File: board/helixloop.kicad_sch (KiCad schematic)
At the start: 17 parts, among them J1 Conn_01x04, J2 Conn_01x02

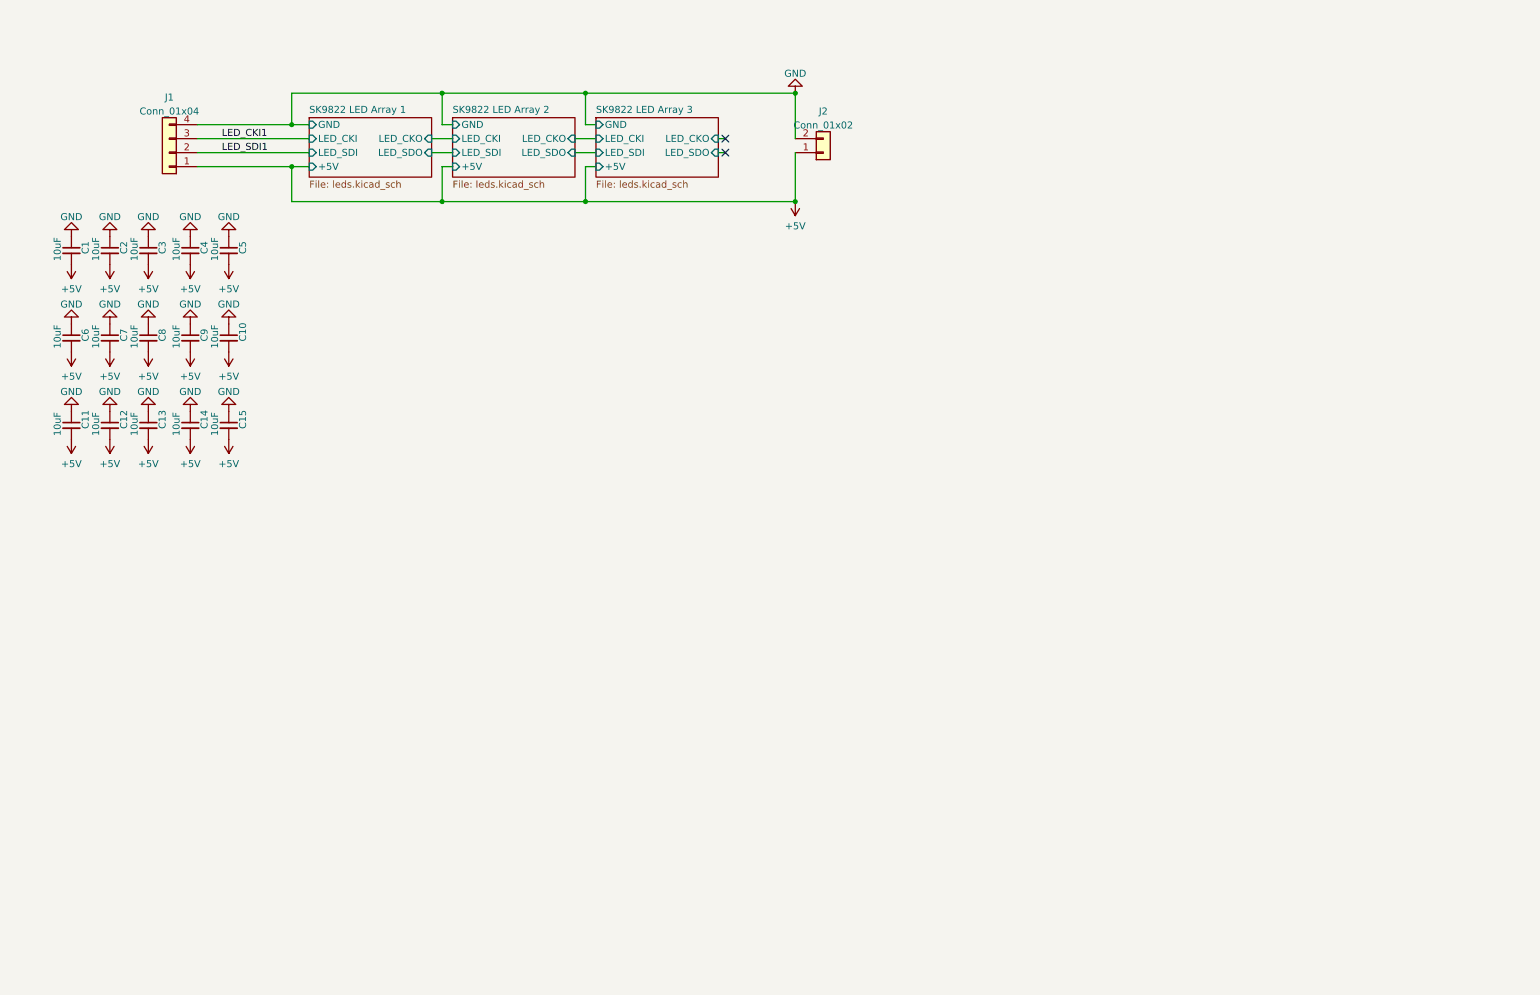
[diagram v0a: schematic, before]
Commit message: v2 concept: add an rp2040, microphone, usb port; rotate entire design 1/12 turn to help align usb port and led data in; rough layout
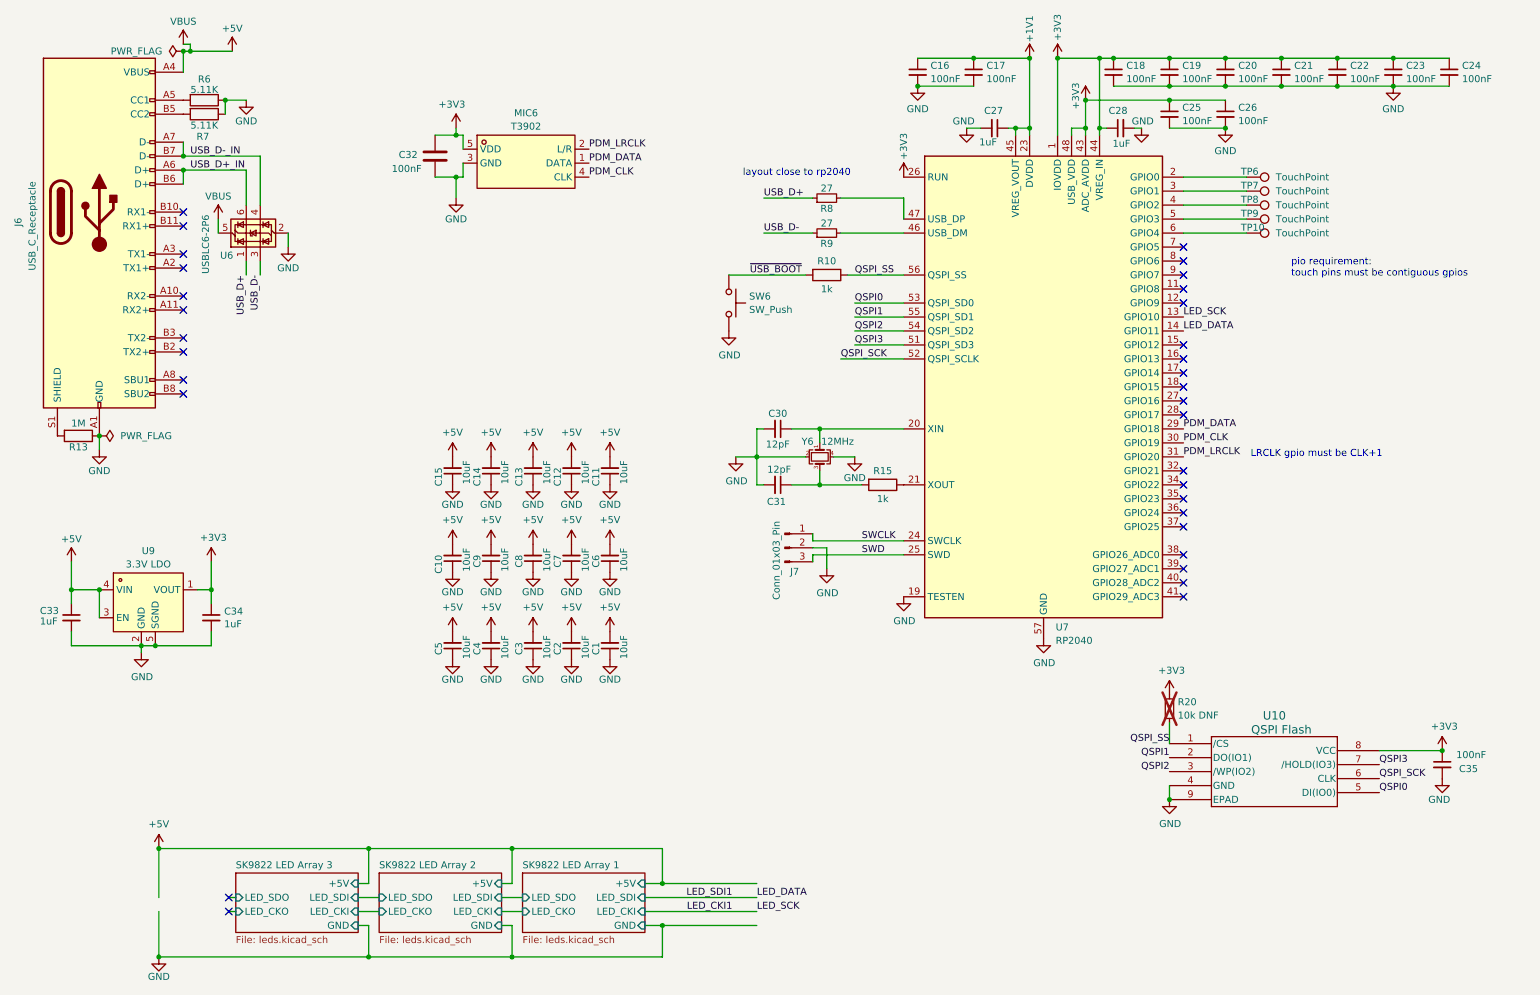
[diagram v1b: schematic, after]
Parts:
- removed J1: Conn_01x04, helixloop:SMD_Pad_01x04_2.54mm, symbol Connector_Generic:Conn_01x04
- removed J2: Conn_01x02, helixloop:SMD_Pad_01x02_2.54mm, symbol Connector_Generic:Conn_01x02
- added C16, C17, C18, C19, C20, C21, C22, C23, C24, C25, C26, C35: 100nF, Capacitor_SMD:C_0402_1005Metric, symbol Device:C_Small
- added C27, C28, C33, C34: 1uF, Capacitor_SMD:C_0402_1005Metric, symbol Device:C_Small
- added C30, C31: 12pF, Capacitor_SMD:C_0402_1005Metric, symbol Device:C_Small
- added C32: 100nF, Capacitor_SMD:C_0402_1005Metric, symbol Device:C
- added J6: USB_C_Receptacle, helixloop:USB-SMD_USB-TYPE-C-020, symbol Connector:USB_C_Receptacle
- added J7: Conn_01x03_Pin, penta:SMD_Pad_01x03_1.27mm, symbol Connector:Conn_01x03_Pin
- added MIC6: T3902, helixloop:MIC_T3902, symbol penta:MMICT390200012
- added R10, R15: 1k, Resistor_SMD:R_0402_1005Metric, symbol Device:R
- added R13: 1M, Resistor_SMD:R_0402_1005Metric, symbol Device:R
- added R20: 10k DNF, Resistor_SMD:R_0402_1005Metric, symbol Device:R_Small
- added R6, R7: 5.11K, Resistor_SMD:R_0402_1005Metric, symbol Device:R
- added R8, R9: 27, Resistor_SMD:R_0402_1005Metric, symbol Device:R_Small
- added SW6: SW_Push, helixloop:KEY-SMD_L3.0-W2.5-LS4.0, symbol Switch:SW_Push
- added TP10, TP6, TP7, TP8, TP9: TouchPoint, penta:ScrewTouchHole, symbol Connector:TestPoint
- added U10: QSPI Flash, helixloop:USON_3X2_WIN, symbol helixloop:QSPI Flash
- added U6: USBLC6-2P6, Package_TO_SOT_SMD:SOT-666, symbol Power_Protection:USBLC6-2P6
- added U7: RP2040, Package_DFN_QFN:QFN-56-1EP_7x7mm_P0.4mm_EP3.2x3.2mm, symbol MCU_RaspberryPi:RP2040
- added U9: 3.3V LDO, Package_DFN_QFN:OnSemi_XDFN4-1EP_1.0x1.0mm_EP0.52x0.52mm, symbol helixloop:RT9078-33GQZ
- added Y6: 12MHz, Crystal:Crystal_SMD_2520-4Pin_2.5x2.0mm, symbol Device:Crystal_GND24_Small
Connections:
- net +5V: now also C33.1, J6.A4 (VBUS), J6.A9 (VBUS), J6.B4 (VBUS), J6.B9 (VBUS), U6.5 (VBUS), U9.3 (EN), U9.4 (VIN)
- net GND: now also C16.2, C17.2, C18.2, C19.2, C20.2, C21.2, C22.2, C23.2, C24.2, C25.2, C26.2, C27.2, C28.2, C30.2, C31.2, C32.2, C33.2, C34.2, C35.2, J6.A1 (GND), J6.A12 (GND), J6.B1 (GND), J6.B12 (GND), J7.2 (Pin_2), MIC6.3 (GND), R13.1, R6.1, R7.1, SW6.2, U10.4 (GND), U10.9 (EPAD), U6.2 (GND), U7.19 (TESTEN), U7.57 (GND), U9.2 (GND), U9.5 (SGND), Y6.2, Y6.4
- net LED_CKI1: now also U7.13 (GPIO10)
- new net: TP7.1, U7.3 (GPIO1)
- new net: C31.1, R15.2, Y6.3
- new net: TP10.1, U7.6 (GPIO4)
- new net: TP6.1, U7.2 (GPIO0)
- new net: C30.1, U7.20 (XIN), Y6.1
- new net: R15.1, U7.21 (XOUT)
- new net: TP8.1, U7.4 (GPIO2)
- new net: R9.2, U7.46 (USB_DM)
- new net: R8.2, U7.47 (USB_DP)
- new net: TP9.1, U7.5 (GPIO3)
- new net: J6.B5 (CC2), R7.2
- new net: J6.S1 (SHIELD), R13.2
- new net: J6.A5 (CC1), R6.2
- new net +1V1: C16.1, C17.1, C27.1, U7.23 (DVDD), U7.45 (VREG_VOUT), U7.50 (DVDD)
- new net +3V3: C18.1, C19.1, C20.1, C21.1, C22.1, C23.1, C24.1, C25.1, C26.1, C28.1, C32.1, C34.1, C35.1, MIC6.5 (VDD), R20.1, U10.8 (VCC), U7.1 (IOVDD), U7.10 (IOVDD), U7.22 (IOVDD), U7.26 (RUN), U7.33 (IOVDD), U7.42 (IOVDD), U7.43 (ADC_AVDD), U7.44 (VREG_IN), U7.48 (USB_VDD), U7.49 (IOVDD), U9.1 (VOUT)
- new net LED_DATA: U7.14 (GPIO11)
- new net PDM_CLK: MIC6.4 (CLK), U7.30 (GPIO19)
- new net PDM_DATA: MIC6.1 (DATA), U7.29 (GPIO18)
- new net PDM_LRCLK: MIC6.2 (L/R), U7.31 (GPIO20)
- new net QSPI0: U10.5 (DI(IO0)), U7.53 (QSPI_SD0)
- new net QSPI1: U10.2 (DO(IO1)), U7.55 (QSPI_SD1)
- new net QSPI2: U10.3 (/WP(IO2)), U7.54 (QSPI_SD2)
- new net QSPI3: U10.7 (/HOLD(IO3)), U7.51 (QSPI_SD3)
- new net QSPI_SCK: U10.6 (CLK), U7.52 (QSPI_SCLK)
- new net QSPI_SS: R10.1, R20.2, U10.1 (/CS), U7.56 (QSPI_SS)
- new net SWCLK: J7.1 (Pin_1), U7.24 (SWCLK)
- new net SWD: J7.3 (Pin_3), U7.25 (SWD)
- new net USB_D+: R8.1, U6.1 (I/O1)
- new net USB_D+_IN: J6.A6 (D+), J6.B6 (D+), U6.6 (I/O1)
- new net USB_D-: R9.1, U6.3 (I/O2)
- new net USB_D-_IN: J6.A7 (D-), J6.B7 (D-), U6.4 (I/O2)
- new net ~{USB_BOOT}: R10.2, SW6.1
- no-connect marks 2 -> 32
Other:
- note added: "LRCLK gpio must be CLK+1"
- note added: "layout close to rp2040"
- note added: "pio requirement: touch pins must be contiguous gpios"
- moved on the sheet: C1, C10, C11, C12, C13, C14, C15, C2, C3, C4, C5, C6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

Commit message: add a 5v copper layer on top; add more 5v capacitance; layout improvements
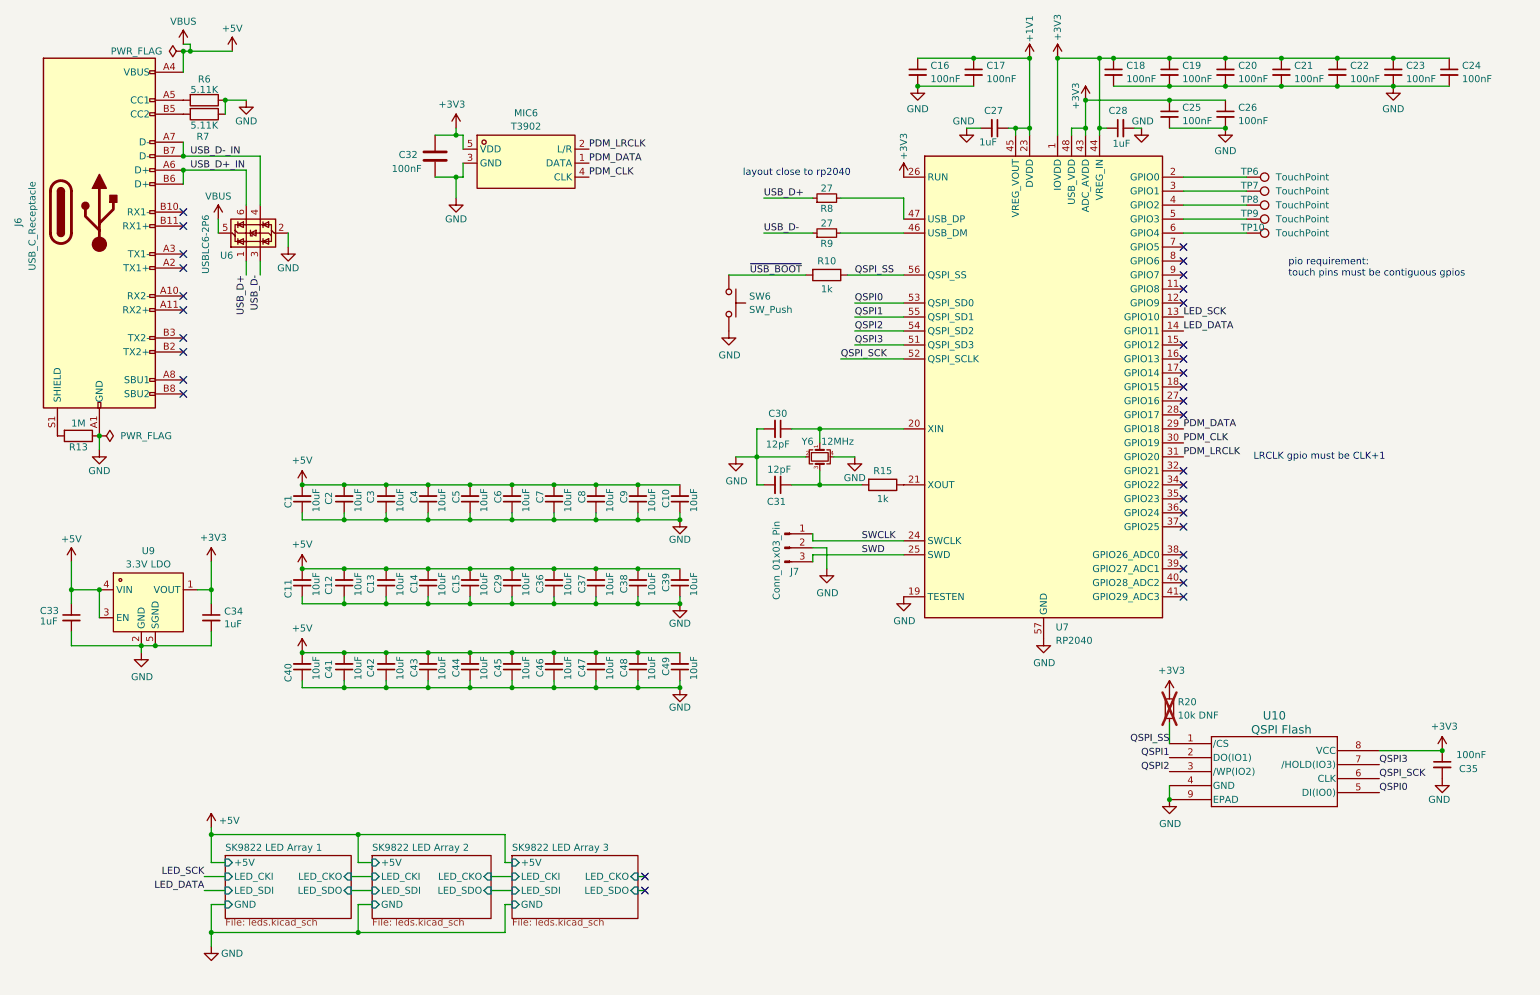
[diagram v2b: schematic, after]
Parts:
- removed C1, C2, C3, C4, C5: 10uF, Capacitor_SMD:C_0402_1005Metric, symbol Device:C_Small
- added C11, C12, C13, C14, C15, C29, C36, C37, C38, C39, C40, C41, C42, C43, C44, C45, C46, C47, C48, C49: 10uF, Capacitor_SMD:C_0402_1005Metric, symbol Device:C_Small
- renumbered C15 to C1, C14 to C2, C13 to C3, C12 to C4, C11 to C5
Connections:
- net +5V: now also C11.2, C12.2, C13.2, C14.2, C15.2, C29.2, C36.2, C37.2, C38.2, C39.2, C40.2, C41.2, C42.2, C43.2, C44.2, C45.2, C46.2, C47.2, C48.2, C49.2
- net GND: now also C11.1, C12.1, C13.1, C14.1, C15.1, C29.1, C36.1, C37.1, C38.1, C39.1, C40.1, C41.1, C42.1, C43.1, C44.1, C45.1, C46.1, C47.1, C48.1, C49.1
- net LED_CKI1 renamed LED_SCK
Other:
- moved on the sheet: C1, C2, C3, C4, C5

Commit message: mostly fix ERC
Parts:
- removed C32: 100nF, Capacitor_SMD:C_0402_1005Metric, symbol Device:C
- removed TP6, TP7: TouchPoint, penta:ScrewTouchHole, symbol Connector:TestPoint
- added C32: 100nF, Capacitor_SMD:C_0402_1005Metric, symbol Device:C_Small
- MIC6: footprint helixloop:MIC_T3902 -> easyeda2kicad:MIC-SMD_5P-L3.5-W2.7-TL_MMICT390200012; symbol penta:MMICT390200012 -> helixloop:MMICT390200012
- TP1: renamed from TP8; footprint penta:ScrewTouchHole -> TestPoint:TestPoint_Pad_D2.5mm
- TP2: renamed from TP9; footprint penta:ScrewTouchHole -> TestPoint:TestPoint_Pad_D2.5mm
- TP3: renamed from TP10; footprint penta:ScrewTouchHole -> TestPoint:TestPoint_Pad_D2.5mm
- U9: value 3.3V LDO -> RT9078
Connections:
- net +3V3: now also C32.1
- net GND: now also C32.2
- net at U7.3 (GPIO1): now also TP2.1
- net at TP3.1: now also U7.4 (GPIO2); no longer U7.6 (GPIO4)
- net at U7.2 (GPIO0): now also TP1.1
- net at U7.5 (GPIO3): no longer TP2.1
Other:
- moved on the sheet: TP1, TP2, TP3, U6
